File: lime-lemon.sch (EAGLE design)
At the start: 96 parts, among them Q1 BSZ105N04NS

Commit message: adds corrections to lime-lemon
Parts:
- removed C16: (no value), rcl:C-EUC0805
- removed R51, R54, R59: (no value), rcl:R-US_R0805
- added CRST: 22n, rcl:C-EUC0805
- added RSENSE: 0.06, rcl:R-US_R0805
- CBOOT, CVCC: value (none) -> 100n
- CCOMP3: value (none) -> 300p
- COUT: value (none) -> 22u
- COUTX: value (none) -> 1u
- CRAMP: value (none) -> 180p
- RCOMP2: value (none) -> 7.87k
- RFBT: value (none) -> 36.5k
- RRAMP: value (none) -> 43k
- renumbered C10 to CBOOT, C11 to CRAMP, C12 to CCOMP3, C14 to CVCC, C17 to COUTX, C6 to COUT, C8 to CIO, R49 to RRAMP, R57 to RFBT, R58 to RCOMP2
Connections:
- removed net N$55: C16.1, U$2.DITH
- net GND: now also CCOMP3.1, U$2.OUT
- net N$52: now also D2.A, RSENSE.1, U$2.CS; no longer CRAMP.1, R51.2, RRAMP.2
- net N$53: now also RRAMP.2; no longer R51.1
- net N$57: no longer R59.2
- net N$60: now also CRST.2, U$2.DITH; no longer R54.2, U$2.CS
- net VDD: now also CRST.1, RSENSE.2; no longer C16.2, CCOMP3.1, D2.A, R59.1, U$1.P$11, U$2.OUT

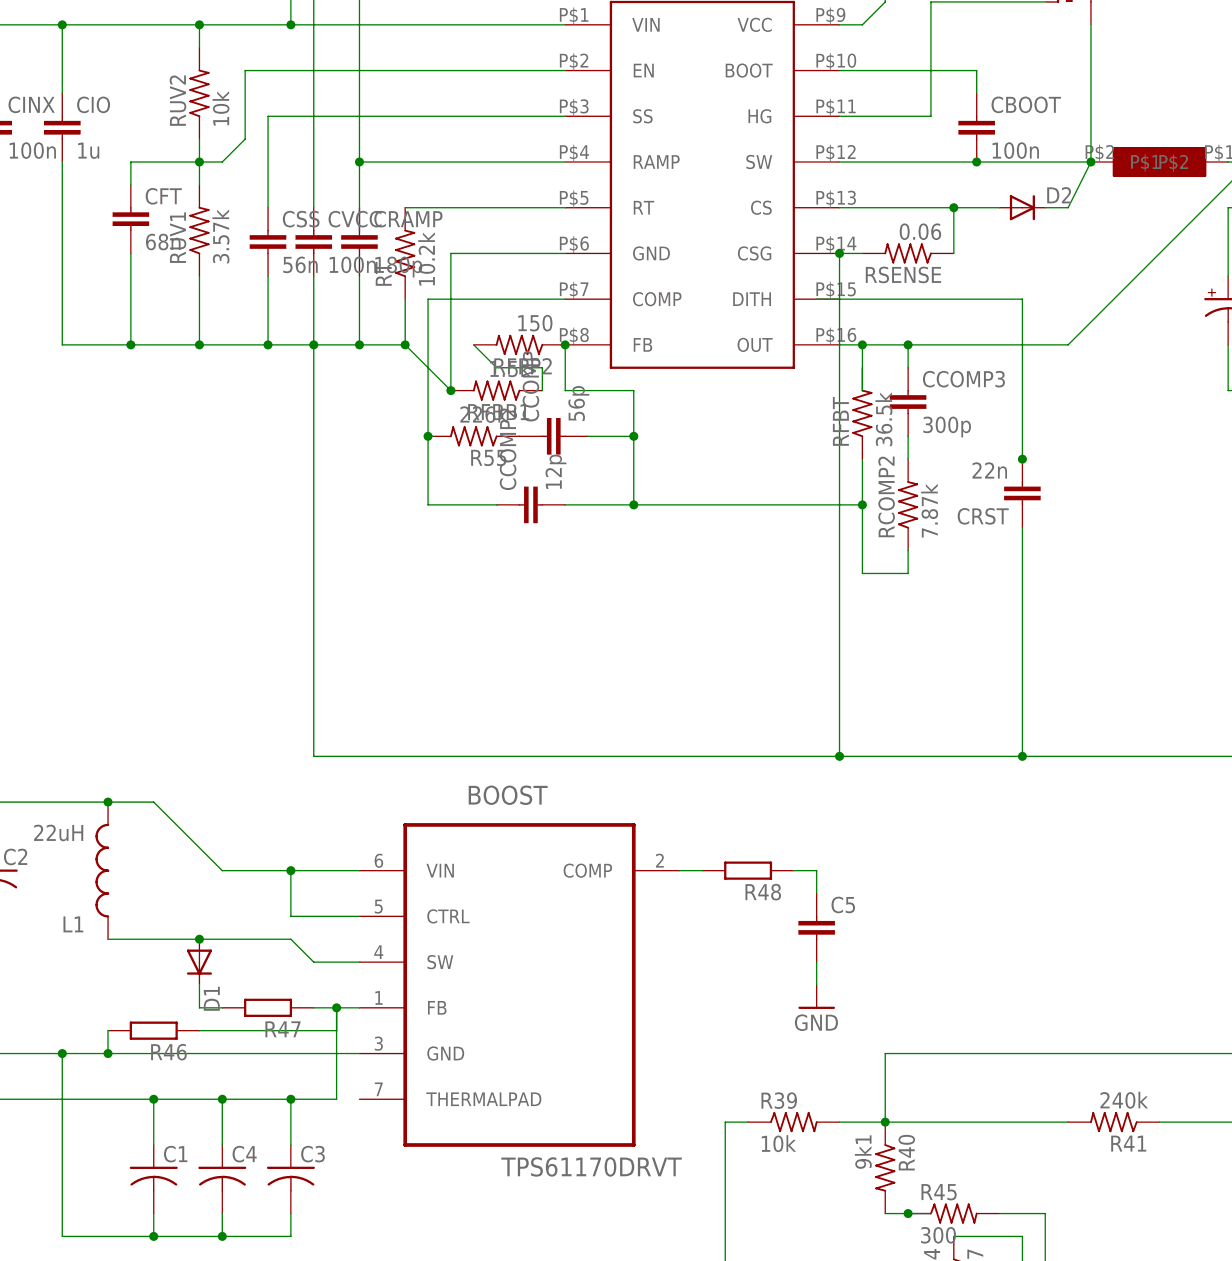
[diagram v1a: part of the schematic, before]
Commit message: add negative voltage booster to lime-lemon
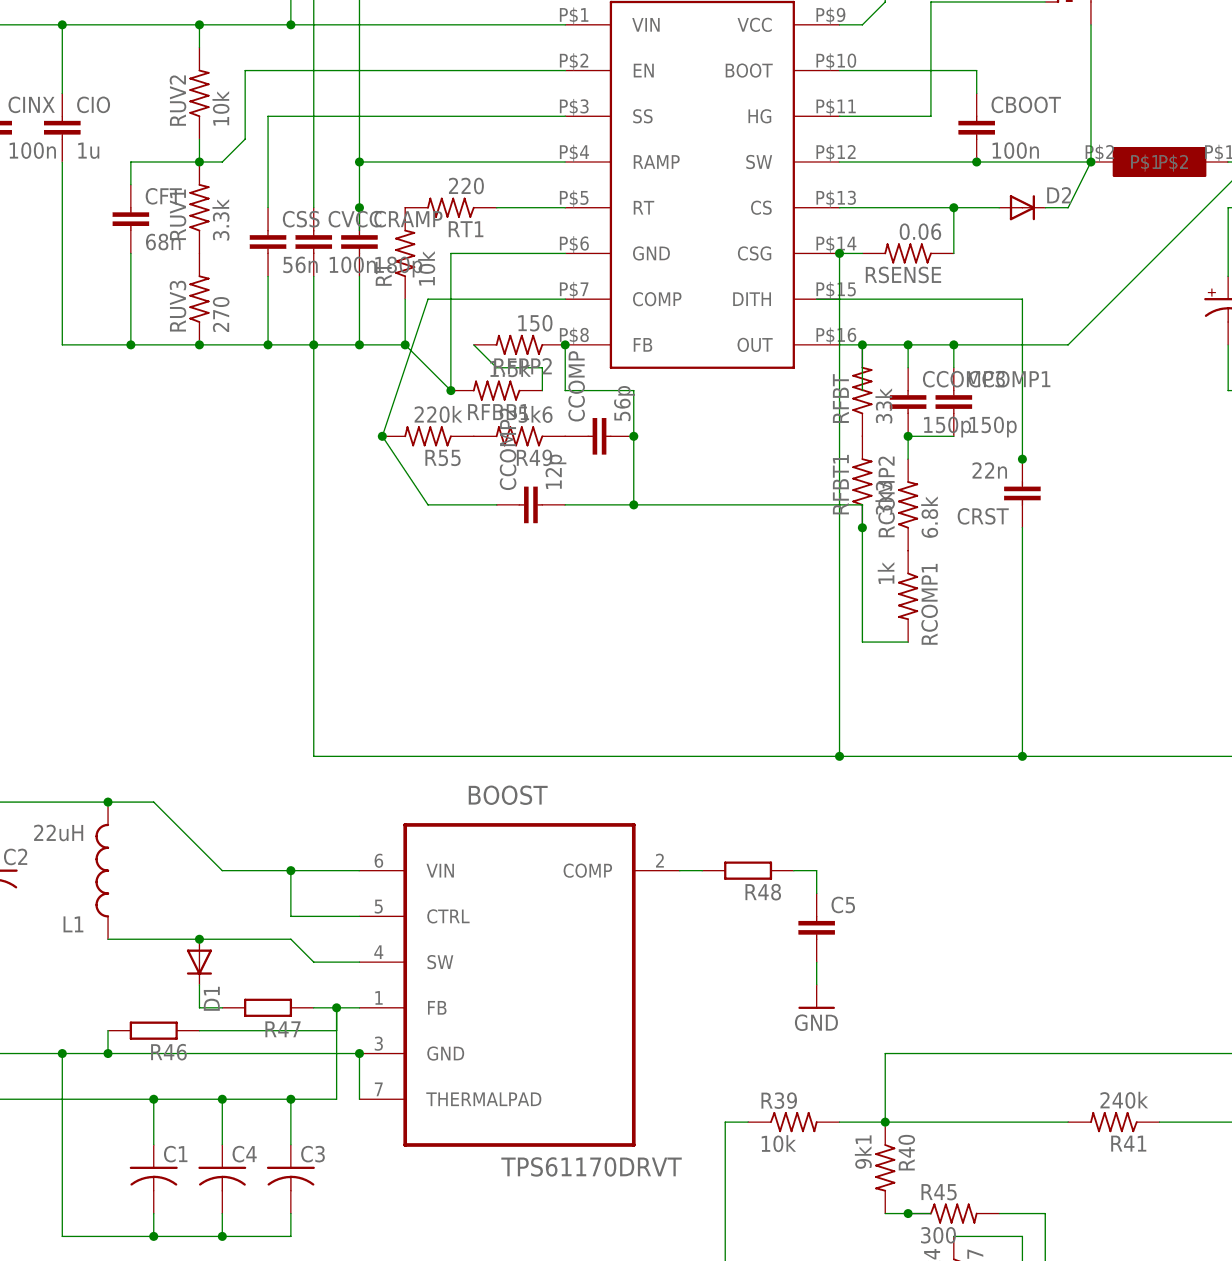
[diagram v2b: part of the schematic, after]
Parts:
- added CCOMP1: 150p, rcl:C-EUC0805
- added R49: 5k6, rcl:R-US_R0805
- added RCOMP1: 1k, rcl:R-US_R0805
- added RFBT1: 3k3, rcl:R-US_R0805
- added RT1: 220, rcl:R-US_R0805
- added RUV3: 270, rcl:R-US_R0805
- CCOMP3: value 300p -> 150p
- R55: value 226k -> 220k
- RCOMP2: value 7.87k -> 6.8k
- RFBT: value 36.5k -> 33k
- RT: value 10.2k -> 10k
- RUV1: value 3.57k -> 3.3k
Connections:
- new net N$55: RUV1.1, RUV3.2
- new net N$66: R49.2, R55.1
- new net N$72: RT1.1, U$2.RT
- new net N$73: RCOMP1.1, RCOMP2.1
- new net N$74: RFBT.1, RFBT1.2
- net GND: now also BOOST.THERMALPAD, CCOMP1.1, RFBT.2
- net N$53: now also CRAMP.1
- net N$54: now also RT1.2; no longer U$2.RT
- net N$56: now also R49.1; no longer R55.1
- net N$57: now also RCOMP1.2, RFBT1.1; no longer RCOMP2.1, RFBT.1
- net N$71: now also CCOMP1.2
- net VDD: now also RUV3.1; no longer RUV1.1
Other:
- moved on the sheet: CCOMP, R55, RFBT, RUV1

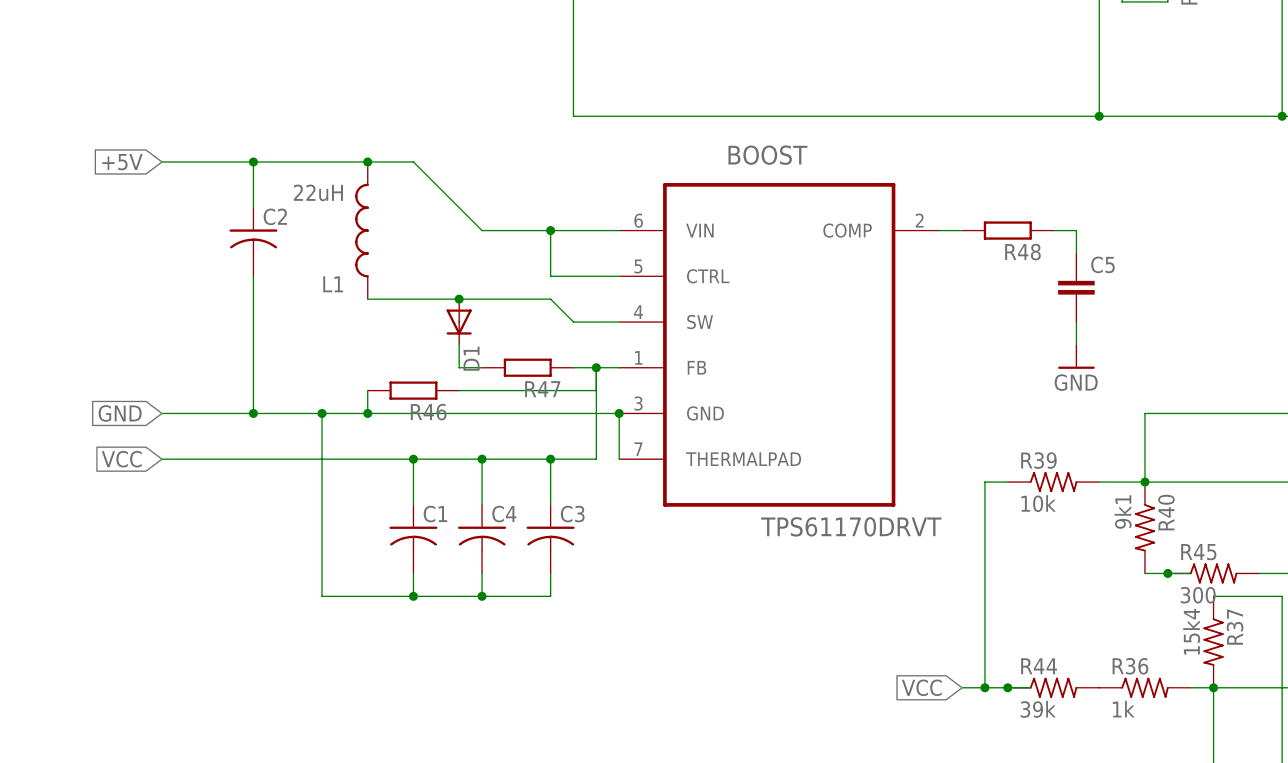
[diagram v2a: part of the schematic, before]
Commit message: Finishes the lime-lemon board
makes the lime-lemon board complete and ready for manufacturing
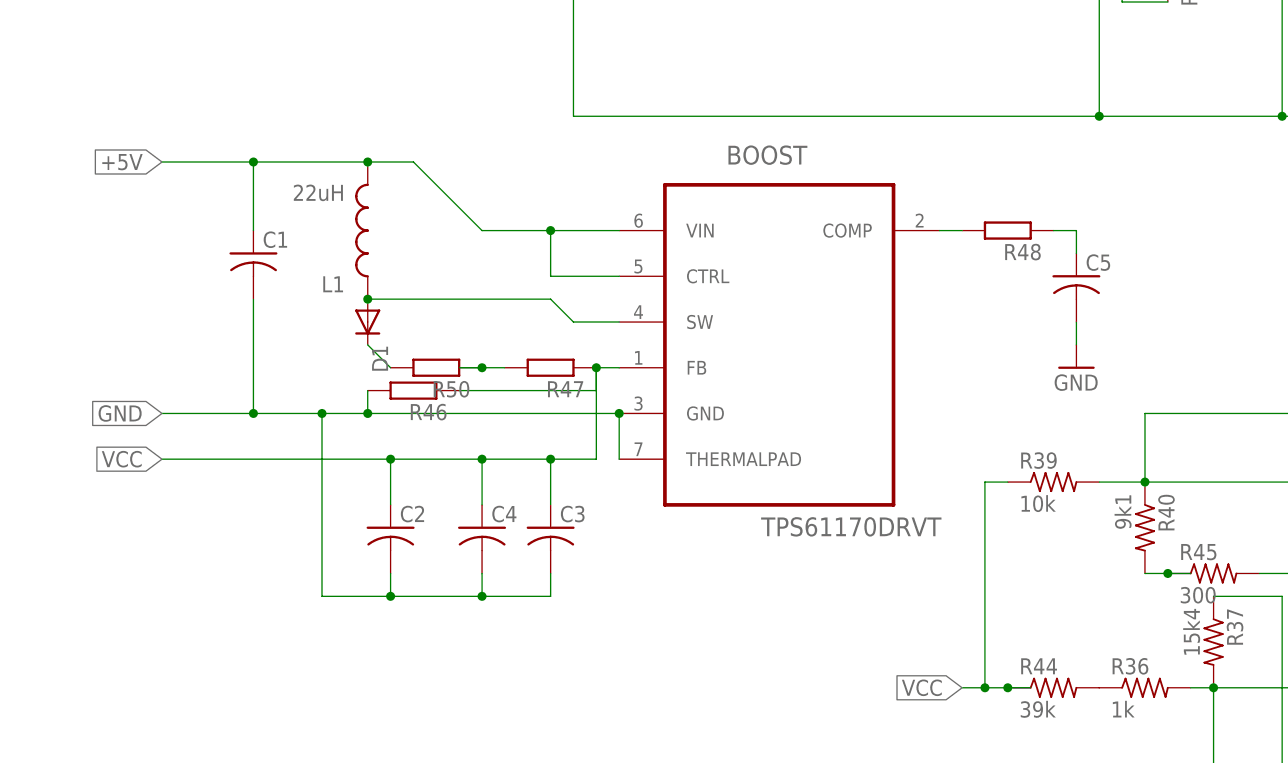
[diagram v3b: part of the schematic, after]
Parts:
- added R50: (no value), rcl:R-EU_R0805
- C5: device rcl:C-EUC0805 -> rcl:C-USC1206
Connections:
- new net N$75: D1.C, R50.2
- net +5V: now also C1.1; no longer C2.1
- net N$47: now also R50.1; no longer D1.C
- net VCC: now also C2.1; no longer C1.1
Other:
- moved on the sheet: C1, C2, D1, R47
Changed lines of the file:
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@@
 <part name="C3" library="rcl" deviceset="C-US" device="C1206"/>
 <part name="C4" library="rcl" deviceset="C-US" device="C1206"/>
-<part name="C5" library="rcl" deviceset="C-EU" device="C0805"/>
 <part name="R46" library="rcl" deviceset="R-EU_" device="R0805"/>
 <part name="R47" library="rcl" deviceset="R-EU_" device="R0805"/>
@@
 <part name="RCOMP1" library="rcl" deviceset="R-US_" device="R0805" value="1k"/>
 <part name="RFBT1" library="rcl" deviceset="R-US_" device="R0805" value="3k3"/>
+<part name="C5" library="rcl" deviceset="C-US" device="C1206"/>
+<part name="R50" library="rcl" deviceset="R-EU_" device="R0805"/>
 </parts>
 <sheets>
@@
 <instance part="SUPPLY2" gate="VDD" x="-68.58" y="-20.32" rot="R180"/>
 <instance part="BOOST" gate="A" x="-38.1" y="124.46"/>
-<instance part="C1" gate="G$1" x="-78.74" y="101.6"/>
-<instance part="C2" gate="G$1" x="-96.52" y="134.62"/>
+<instance part="C1" gate="G$1" x="-96.52" y="132.08"/>
+<instance part="C2" gate="G$1" x="-81.28" y="101.6"/>
 <instance part="C3" gate="G$1" x="-63.5" y="101.6"/>
 <instance part="C4" gate="G$1" x="-71.12" y="101.6"/>
-<instance part="C5" gate="G$1" x="-5.08" y="129.54"/>
 <instance part="R46" gate="G$1" x="-78.74" y="116.84" rot="R180"/>
-<instance part="R47" gate="G$1" x="-66.04" y="119.38" rot="R180"/>
+<instance part="R47" gate="G$1" x="-63.5" y="119.38" rot="R180"/>
 <instance part="R48" gate="G$1" x="-12.7" y="134.62" rot="R180"/>
 <instance part="L1" gate="G$1" x="-83.82" y="134.62" rot="R180"/>
-<instance part="D1" gate="G$1" x="-73.66" y="124.46" rot="R270"/>
+<instance part="D1" gate="G$1" x="-83.82" y="124.46" rot="R270"/>
 <instance part="GND3" gate="1" x="-5.08" y="119.38"/>
 <instance part="U$2" gate="G$1" x="-17.78" y="210.82"/>
@@
 <instance part="RCOMP1" gate="G$1" x="5.08" y="165.1" rot="R270"/>
 <instance part="RFBT1" gate="G$1" x="0" y="177.8" rot="R90"/>
+<instance part="C5" gate="G$1" x="-5.08" y="129.54"/>
+<instance part="R50" gate="G$1" x="-76.2" y="119.38" rot="R180"/>
 </instances>
 <busses>
@@
 </segment>
 <segment>
-<pinref part="C5" gate="G$1" pin="2"/>
 <pinref part="GND3" gate="1" pin="GND"/>
 <wire x1="-5.08" y1="124.46" x2="-5.08" y2="121.92" width="0.1524" layer="91"/>
-</segment>
-<segment>
-<pinref part="C2" gate="G$1" pin="2"/>
-<wire x1="-96.52" y1="114.3" x2="-96.52" y2="129.54" width="0.1524" layer="91"/>
+<pinref part="C5" gate="G$1" pin="2"/>
+</segment>
+<segment>
 <pinref part="BOOST" gate="A" pin="GND"/>
 <wire x1="-55.88" y1="114.3" x2="-83.82" y2="114.3" width="0.1524" layer="91"/>
 <pinref part="R46" gate="G$1" pin="2"/>
 <wire x1="-83.82" y1="114.3" x2="-83.82" y2="116.84" width="0.1524" layer="91"/>
-<wire x1="-96.52" y1="114.3" x2="-88.9" y2="114.3" width="0.1524" layer="91"/>
 <junction x="-83.82" y="114.3"/>
 <wire x1="-88.9" y1="114.3" x2="-83.82" y2="114.3" width="0.1524" layer="91"/>
+<wire x1="-88.9" y1="114.3" x2="-96.52" y2="114.3" width="0.1524" layer="91"/>
+<label x="-106.68" y="114.3" size="1.778" layer="95" rot="R180" xref="yes"/>
 <wire x1="-96.52" y1="114.3" x2="-106.68" y2="114.3" width="0.1524" layer="91"/>
-<junction x="-96.52" y="114.3"/>
-<label x="-106.68" y="114.3" size="1.778" layer="95" rot="R180" xref="yes"/>
 <wire x1="-88.9" y1="93.98" x2="-88.9" y2="114.3" width="0.1524" layer="91"/>
 <junction x="-88.9" y="114.3"/>
@@
 <pinref part="C3" gate="G$1" pin="2"/>
 <wire x1="-63.5" y1="96.52" x2="-63.5" y2="93.98" width="0.1524" layer="91"/>
-<wire x1="-88.9" y1="93.98" x2="-78.74" y2="93.98" width="0.1524" layer="91"/>
+<wire x1="-88.9" y1="93.98" x2="-81.28" y2="93.98" width="0.1524" layer="91"/>
 <junction x="-71.12" y="93.98"/>
-<pinref part="C1" gate="G$1" pin="2"/>
-<wire x1="-78.74" y1="93.98" x2="-71.12" y2="93.98" width="0.1524" layer="91"/>
-<wire x1="-78.74" y1="96.52" x2="-78.74" y2="93.98" width="0.1524" layer="91"/>
-<junction x="-78.74" y="93.98"/>
 <pinref part="BOOST" gate="A" pin="THERMALPAD"/>
+<wire x1="-81.28" y1="93.98" x2="-71.12" y2="93.98" width="0.1524" layer="91"/>
 <wire x1="-55.88" y1="109.22" x2="-55.88" y2="114.3" width="0.1524" layer="91"/>
 <junction x="-55.88" y="114.3"/>
+<pinref part="C1" gate="G$1" pin="2"/>
+<wire x1="-96.52" y1="127" x2="-96.52" y2="114.3" width="0.1524" layer="91"/>
+<junction x="-96.52" y="114.3"/>
+<pinref part="C2" gate="G$1" pin="2"/>
+<wire x1="-81.28" y1="96.52" x2="-81.28" y2="93.98" width="0.1524" layer="91"/>
+<junction x="-81.28" y="93.98"/>
 </segment>
 <segment>
@@
 <pinref part="R47" gate="G$1" pin="1"/>
 <pinref part="BOOST" gate="A" pin="FB"/>
-<wire x1="-60.96" y1="119.38" x2="-58.42" y2="119.38" width="0.1524" layer="91"/>
 <wire x1="-58.42" y1="119.38" x2="-55.88" y2="119.38" width="0.1524" layer="91"/>
 <wire x1="-58.42" y1="119.38" x2="-58.42" y2="116.84" width="0.1524" layer="91"/>
@@
 <wire x1="-58.42" y1="119.38" x2="-58.42" y2="109.22" width="0.1524" layer="91"/>
 <wire x1="-58.42" y1="109.22" x2="-63.5" y2="109.22" width="0.1524" layer="91"/>
-<pinref part="C1" gate="G$1" pin="1"/>
 <wire x1="-63.5" y1="109.22" x2="-71.12" y2="109.22" width="0.1524" layer="91"/>
-<wire x1="-71.12" y1="109.22" x2="-78.74" y2="109.22" width="0.1524" layer="91"/>
-<wire x1="-78.74" y1="109.22" x2="-78.74" y2="104.14" width="0.1524" layer="91"/>
 <pinref part="C4" gate="G$1" pin="1"/>
 <wire x1="-71.12" y1="109.22" x2="-71.12" y2="104.14" width="0.1524" layer="91"/>
@@
 <wire x1="-63.5" y1="109.22" x2="-63.5" y2="104.14" width="0.1524" layer="91"/>
 <junction x="-63.5" y="109.22"/>
-<junction x="-78.74" y="109.22"/>
-<wire x1="-78.74" y1="109.22" x2="-106.68" y2="109.22" width="0.1524" layer="91"/>
+<wire x1="-71.12" y1="109.22" x2="-81.28" y2="109.22" width="0.1524" layer="91"/>
 <label x="-106.68" y="109.22" size="1.778" layer="95" rot="R180" xref="yes"/>
+<pinref part="C2" gate="G$1" pin="1"/>
+<wire x1="-81.28" y1="109.22" x2="-106.68" y2="109.22" width="0.1524" layer="91"/>
+<wire x1="-81.28" y1="104.14" x2="-81.28" y2="109.22" width="0.1524" layer="91"/>
+<junction x="-81.28" y="109.22"/>
 </segment>
 </net>
@@
 <wire x1="-71.12" y1="134.62" x2="-78.74" y2="142.24" width="0.1524" layer="91"/>
 <pinref part="L1" gate="G$1" pin="2"/>
+<wire x1="-106.68" y1="142.24" x2="-96.52" y2="142.24" width="0.1524" layer="91"/>
 <wire x1="-96.52" y1="142.24" x2="-83.82" y2="142.24" width="0.1524" layer="91"/>
-<pinref part="C2" gate="G$1" pin="1"/>
-<wire x1="-96.52" y1="137.16" x2="-96.52" y2="142.24" width="0.1524" layer="91"/>
 <wire x1="-78.74" y1="142.24" x2="-83.82" y2="142.24" width="0.1524" layer="91"/>
 <junction x="-83.82" y="142.24"/>
-<wire x1="-96.52" y1="142.24" x2="-106.68" y2="142.24" width="0.1524" layer="91"/>
+<label x="-106.68" y="142.24" size="1.778" layer="95" rot="R180" xref="yes"/>
+<pinref part="C1" gate="G$1" pin="1"/>
+<wire x1="-96.52" y1="134.62" x2="-96.52" y2="142.24" width="0.1524" layer="91"/>
 <junction x="-96.52" y="142.24"/>
-<label x="-106.68" y="142.24" size="1.778" layer="95" rot="R180" xref="yes"/>
 </segment>
 <segment>
@@
 <segment>
 <pinref part="L1" gate="G$1" pin="1"/>
-<wire x1="-83.82" y1="127" x2="-73.66" y2="127" width="0.1524" layer="91"/>
 <pinref part="D1" gate="G$1" pin="A"/>
-<wire x1="-73.66" y1="127" x2="-63.5" y2="127" width="0.1524" layer="91"/>
-<junction x="-73.66" y="127"/>
+<wire x1="-83.82" y1="127" x2="-63.5" y2="127" width="0.1524" layer="91"/>
+<junction x="-83.82" y="127"/>
 <wire x1="-63.5" y1="127" x2="-60.96" y2="124.46" width="0.1524" layer="91"/>
 <pinref part="BOOST" gate="A" pin="SW"/>
@@
 <segment>
 <pinref part="R47" gate="G$1" pin="2"/>
+<wire x1="-68.58" y1="119.38" x2="-71.12" y2="119.38" width="0.1524" layer="91"/>
+<pinref part="R50" gate="G$1" pin="1"/>
 <wire x1="-71.12" y1="119.38" x2="-73.66" y2="119.38" width="0.1524" layer="91"/>
-<pinref part="D1" gate="G$1" pin="C"/>
-<wire x1="-73.66" y1="119.38" x2="-73.66" y2="121.92" width="0.1524" layer="91"/>
+<junction x="-71.12" y="119.38"/>
 </segment>
 </net>
@@
 <pinref part="R48" gate="G$1" pin="1"/>
 <wire x1="-7.62" y1="134.62" x2="-5.08" y2="134.62" width="0.1524" layer="91"/>
+<wire x1="-5.08" y1="134.62" x2="-5.08" y2="132.08" width="0.1524" layer="91"/>
 <pinref part="C5" gate="G$1" pin="1"/>
-<wire x1="-5.08" y1="134.62" x2="-5.08" y2="132.08" width="0.1524" layer="91"/>
 </segment>
 </net>
@@
 </segment>
 </net>
+<net name="N$75" class="0">
+<segment>
+<pinref part="R50" gate="G$1" pin="2"/>
+<pinref part="D1" gate="G$1" pin="C"/>
+<wire x1="-81.28" y1="119.38" x2="-83.82" y2="121.92" width="0.1524" layer="91"/>
+</segment>
+</net>
